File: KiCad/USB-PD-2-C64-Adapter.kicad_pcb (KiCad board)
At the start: 2 copper layers, 42.4 x 35.2 mm, 26 parts, among them U1 AP64500SP-13, U2 STEF05SGR, U3 TPS3700DDCR

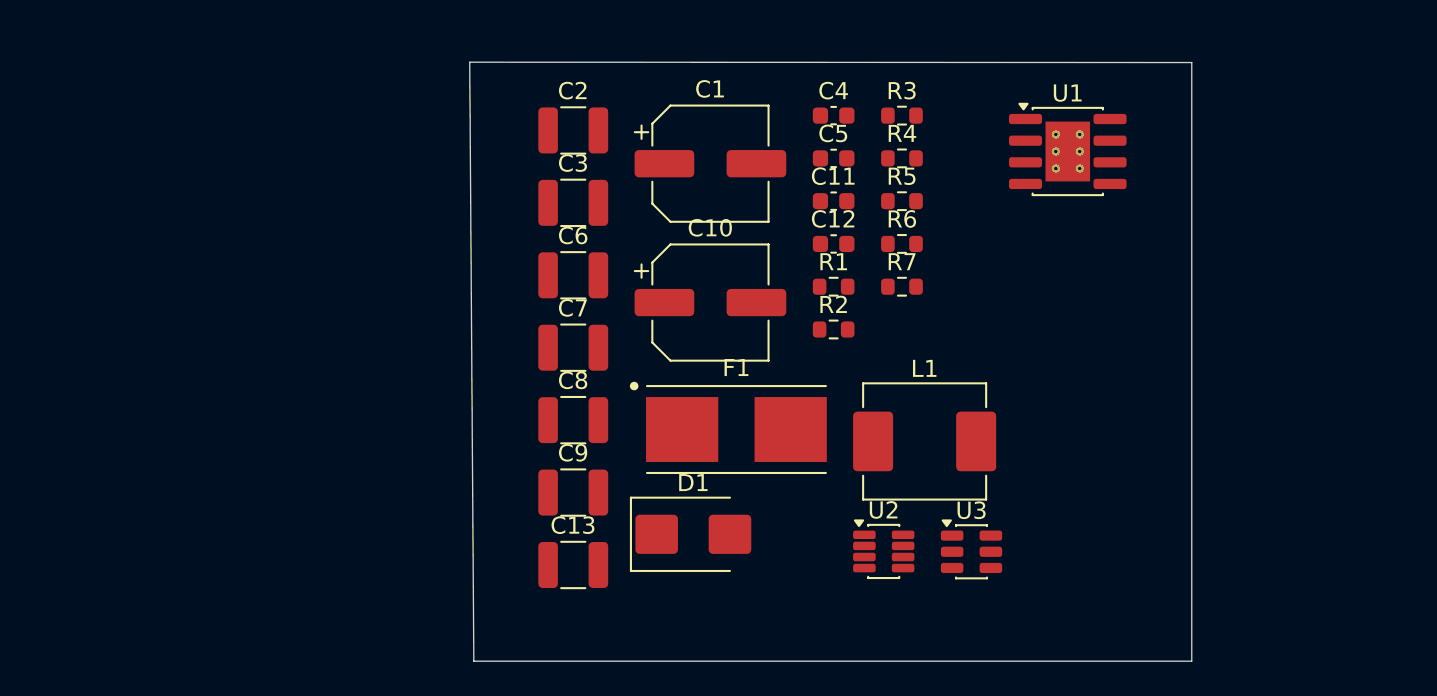
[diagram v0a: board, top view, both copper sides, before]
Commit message: Update USB-PD input protection assets
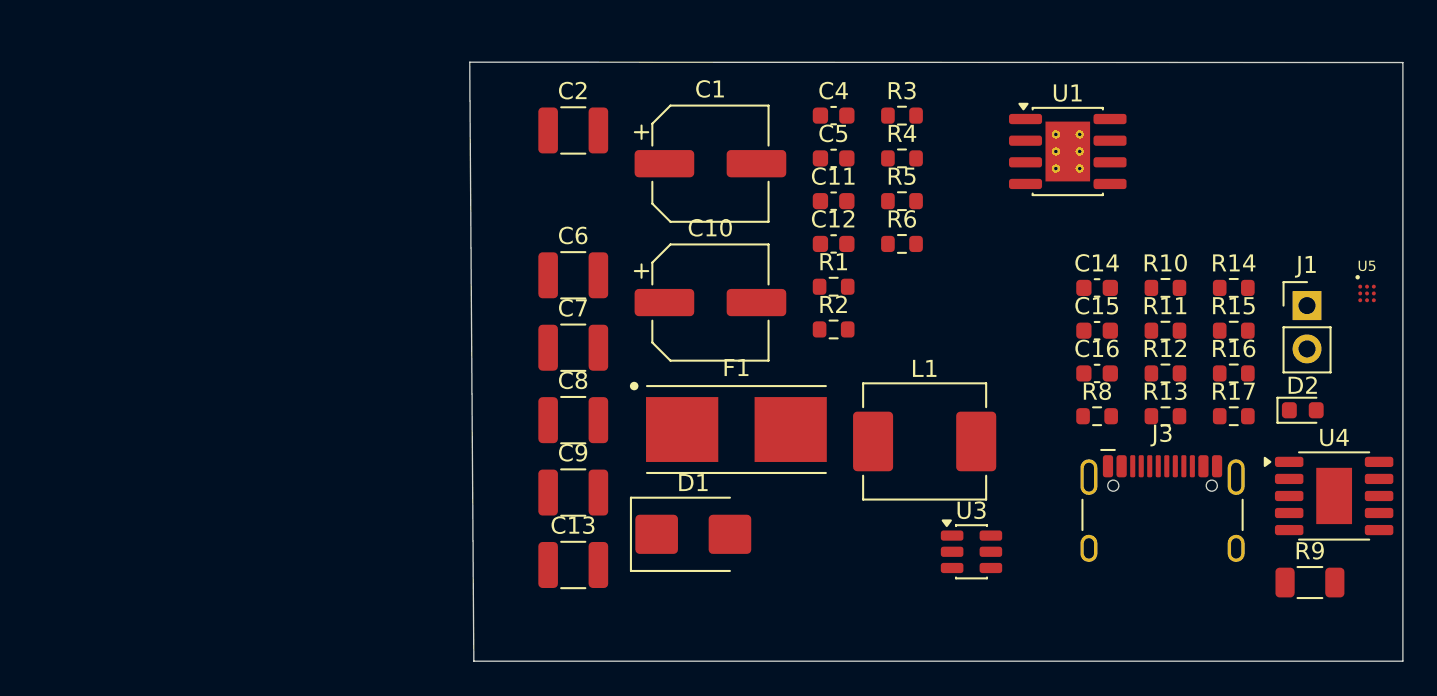
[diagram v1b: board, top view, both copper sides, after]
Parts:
- removed C3: 10uF, Capacitor_SMD:C_1210_3225Metric
- removed R7: 33, Resistor_SMD:R_0603_1608Metric
- removed U2: STEF05SGR, Package_TO_SOT_SMD:TSOT-23-8
- added C14: 1uF X7R 25V, Capacitor_SMD:C_0603_1608Metric, F.Cu at (143.4, 76.8)
- added C15: 100nF X7R 50V, Capacitor_SMD:C_0603_1608Metric, F.Cu at (143.4, 79.3)
- added C16: 22nF X7R 50V, Capacitor_SMD:C_0603_1608Metric, F.Cu at (143.4, 81.8)
- added D2: KT-0603G green, USB-PD-2-C64-Adapter:KT-0603G_C12624, F.Cu at (155.4, 84.0)
- added J1: 2-pin 2.54mm lab/test input DNP, Connector_PinHeader_2.54mm:PinHeader_1x02_P2.54mm_Vertical, F.Cu at (155.7, 77.9)
- added J3: TYPE-C16PIN C393939, USB-PD-2-C64-Adapter:TYPE-C16PIN_C393939, F.Cu at (147.2, 91.0)
- added R10: 2.2k, Resistor_SMD:R_0603_1608Metric, F.Cu at (147.4, 76.8)
- added R11: 1M, Resistor_SMD:R_0603_1608Metric, F.Cu at (147.4, 79.3)
- added R12: 100k, Resistor_SMD:R_0603_1608Metric, F.Cu at (147.4, 81.8)
- added R13: 100k, Resistor_SMD:R_0603_1608Metric, F.Cu at (147.4, 84.4)
- added R14: 274k, Resistor_SMD:R_0603_1608Metric, F.Cu at (151.4, 76.8)
- added R15: 7.68k, Resistor_SMD:R_0603_1608Metric, F.Cu at (151.4, 79.3)
- added R16: 20.0k, Resistor_SMD:R_0603_1608Metric, F.Cu at (151.4, 81.8)
- added R17: 18k, Resistor_SMD:R_0603_1608Metric, F.Cu at (151.4, 84.4)
- added R8: 56k 1%, Resistor_SMD:R_0603_1608Metric, F.Cu at (143.4, 84.4)
- added R9: 1k 1%, Resistor_SMD:R_1206_3216Metric, F.Cu at (155.8, 94.1)
- added U4: CH224K, USB-PD-2-C64-Adapter:CH224K_ESSOP-10-150mil-1mm, F.Cu at (157.3, 89.0)
- added U5: TPD2S300YFFR, USB-PD-2-C64-Adapter:TPD2S300YFFR_DSBGA-9, F.Cu at (159.2, 77.2)
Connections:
- net /VIN_PD_15V renamed Net-(J3-VBUS_A4B9)
- C1 pad 1: /BUCK_EN -> /VIN_BUCK
- C10 pad 1: /5V_RAW -> /5V_PROTECTED_SENSE
- C11 pad 1: /5V_RAW -> /5V_PROTECTED_SENSE
- C2 pad 1: /BUCK_EN -> /VIN_BUCK
- C5 pad 1: /5V_RAW -> /5V_PROTECTED_SENSE
- C6 pad 1: /5V_RAW -> /5V_PROTECTED_SENSE
- C7 pad 1: /5V_RAW -> /5V_PROTECTED_SENSE
- C8 pad 1: /5V_RAW -> /5V_PROTECTED_SENSE
- C9 pad 1: /5V_RAW -> /5V_PROTECTED_SENSE
- D1 pad 2: /BUCK_EN -> /VIN_BUCK
- F1 pad 2: /BUCK_EN -> /VBUS
- L1 pad 2: /5V_RAW -> /5V_PROTECTED_SENSE
- R3 pad 1: /5V_RAW -> /5V_PROTECTED_SENSE
- R5 pad 1: /5V_RAW -> /5V_PROTECTED_SENSE
- U1 pad 2: /BUCK_EN -> /VIN_BUCK
- U3 pad 3: /5V_RAW -> /5V_PROTECTED_SENSE
- U3 pad 5: /5V_RAW -> /5V_PROTECTED_SENSE
- U3 pad 6: Net-(U2-En/Fault) -> /EFUSE_SHDN
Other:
- board size 42.4 x 35.2 mm -> 54.8 x 35.2 mm

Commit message: Update 9VAC design assets
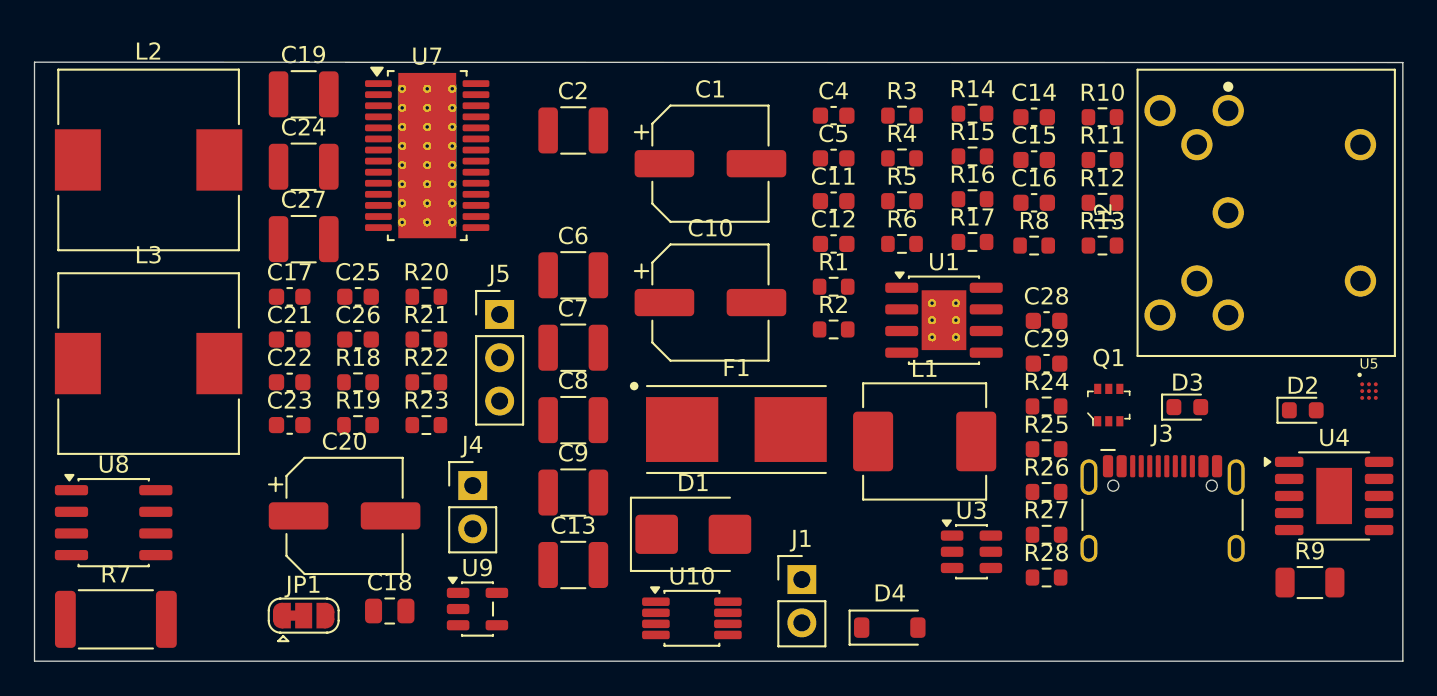
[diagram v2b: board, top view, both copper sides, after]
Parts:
- added C17: 100nF 50V, Capacitor_SMD:C_0603_1608Metric, F.Cu at (96.0, 77.3)
- added C18: 1uF 50V, Capacitor_SMD:C_0805_2012Metric, F.Cu at (101.8, 95.8)
- added C19: 10uF 50V, Capacitor_SMD:C_1210_3225Metric, F.Cu at (96.8, 65.5)
- added C20: 100uF 35V, Capacitor_SMD:CP_Elec_6.3x7.7, F.Cu at (99.2, 90.2)
- added C21: 220nF X7R 50V, Capacitor_SMD:C_0603_1608Metric, F.Cu at (96.0, 79.9)
- added C22: 22nF, Capacitor_SMD:C_0603_1608Metric, F.Cu at (96.0, 82.4)
- added C23: 1uF, Capacitor_SMD:C_0603_1608Metric, F.Cu at (96.0, 84.9)
- added C24: 1uF X7R 50V, Capacitor_SMD:C_1210_3225Metric, F.Cu at (96.8, 69.7)
- added C25: 100nF X7R 50V, Capacitor_SMD:C_0603_1608Metric, F.Cu at (100.0, 77.3)
- added C26: 100nF X7R 50V, Capacitor_SMD:C_0603_1608Metric, F.Cu at (100.0, 79.9)
- added C27: 1uF X7R 50V DNP, Capacitor_SMD:C_1210_3225Metric, F.Cu at (96.8, 74.0)
- added C28: 1uF X7R 25V, Capacitor_SMD:C_0603_1608Metric, F.Cu at (140.4, 78.8)
- added C29: 100nF X7R 50V, Capacitor_SMD:C_0603_1608Metric, F.Cu at (140.4, 81.3)
- added D3: KT-0603R red, LED_SMD:LED_0603_1608Metric, F.Cu at (148.7, 83.8)
- added D4: 1N4148W, Diode_SMD:D_SOD-123, F.Cu at (131.2, 96.8)
- added J2: DIN-704, USB-PD-2-C64-Adapter:DIN-704-M10_C20611695, F.Cu at (152.9, 72.4)
- added J4: 50 / 60Hz, Connector_PinHeader_2.54mm:PinHeader_1x02_P2.54mm_Vertical, F.Cu at (106.7, 88.4)
- added J5: UPDI, Connector_PinHeader_2.54mm:PinHeader_1x03_P2.54mm_Vertical, F.Cu at (108.3, 78.4)
- added JP1: Decay, Jumper:SolderJumper-3_P1.3mm_Bridged12_RoundedPad1.0x1.5mm, F.Cu at (96.8, 96.1)
- added L2: 47uH 5A START, Inductor_SMD:L_10.4x10.4_H4.8, F.Cu at (87.7, 69.3)
- added L3: 47uH 5A START, Inductor_SMD:L_10.4x10.4_H4.8, F.Cu at (87.7, 81.3)
- added Q1: 2N7002DW-7-F, digikey-footprints:SOT-363, F.Cu at (144.0, 83.7)
- added R18: 33, Resistor_SMD:R_0603_1608Metric, F.Cu at (100.0, 82.4)
- added R19: 33, Resistor_SMD:R_0603_1608Metric, F.Cu at (100.0, 84.9)
- added R20: 100k, Resistor_SMD:R_0603_1608Metric, F.Cu at (104.0, 77.3)
- added R21: 10k, Resistor_SMD:R_0603_1608Metric, F.Cu at (104.0, 79.9)
- added R22: 10k 1%, Resistor_SMD:R_0603_1608Metric, F.Cu at (104.0, 82.4)
- added R23: 10k 1%, Resistor_SMD:R_0603_1608Metric, F.Cu at (104.0, 84.9)
- added R24: 4.7k, Resistor_SMD:R_0603_1608Metric, F.Cu at (140.4, 83.8)
- added R25: 100k, Resistor_SMD:R_0603_1608Metric, F.Cu at (140.4, 86.3)
- added R26: 100k, Resistor_SMD:R_0603_1608Metric, F.Cu at (140.4, 88.8)
- added R27: 1k, Resistor_SMD:R_0603_1608Metric, F.Cu at (140.4, 91.3)
- added R28: 4.7k, Resistor_SMD:R_0603_1608Metric, F.Cu at (140.4, 93.8)
- added R7: 10mR 1% 3W SHUNT, Resistor_SMD:R_2512_6332Metric, F.Cu at (85.8, 96.3)
- added U10: SN74LVC2G132DCTR, Package_SO:VSSOP-8_3x3mm_P0.65mm, F.Cu at (119.6, 96.2)
- added U7: DRV8256PPWPR, Package_SO:Texas_PWP0028V_TSSOP-28-1EP_4.4x9.7mm_P0.65mm_EP3.4x9.7mm_Mask2.94x5.62mm_ThermalVias, F.Cu at (104.0, 69.1)
- added U8: ATTINY412-SSNR, Package_SO:SOIC-8_3.9x4.9mm_P1.27mm, F.Cu at (85.6, 90.6)
- added U9: INA180A2IDBVR, Package_TO_SOT_SMD:SOT-23-5, F.Cu at (107.0, 95.7)
- C4: value 100nF BST-SW -> 100nF
- R10: value 2.2k -> 470R
- moved J1 33.7 mm to (126.0, 93.9)
- moved R14 18.4 mm to (136.0, 66.6)
- moved R17 18.4 mm to (136.0, 74.1)
- moved R15 18.4 mm to (136.0, 69.1)
- moved R16 18.4 mm to (136.0, 71.6)
- moved U1 12.3 mm to (134.4, 78.7)
- moved R10 10.7 mm to (143.7, 66.8)
- moved R11 10.7 mm to (143.7, 69.3)
- moved R12 10.7 mm to (143.7, 71.8)
- moved R13 10.7 mm to (143.7, 74.3)
- moved C14 10.7 mm to (139.7, 66.8)
- moved C15 10.7 mm to (139.7, 69.3)
- moved C16 10.7 mm to (139.7, 71.8)
- moved R8 10.7 mm to (139.7, 74.3)
- moved U5 5.73 mm to (159.3, 82.9)
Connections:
- C13 pad 1: /5V_PROTECTED_SENSE -> Net-(J2-5VDC_4)
- D2 pad 2: GND -> Net-(D2-A)
- R10 pad 1: Net-(U4-PG) -> Net-(D2-A)
- R10 pad 2: Net-(D2-K) -> /CH224_VDD_3V3
- U4 pad 10: Net-(U4-PG) -> Net-(D2-K)
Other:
- board size 54.8 x 35.2 mm -> 80.3 x 35.2 mm
